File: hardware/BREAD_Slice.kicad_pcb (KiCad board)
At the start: 2 copper layers, 70 x 100 mm, 38 parts, among them J1 Conn_01x10_Socket, J2 Screw_Terminal_01x04, J3 Screw_Terminal_01x04, J4 Screw_Terminal_01x02, J5 Screw_Terminal_01x02, J6 Screw_Terminal_01x02, J7 Screw_Terminal_01x02, U1 AP63205, U2 LMD18200T_NOPB, U3 LMD18200T_NOPB

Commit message: and a few months later picked up like nothing happened...anyway done
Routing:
- net GNDPWR: track 42.2 -> 54.8 mm
- net GND: track 16.8 -> 27.3 mm, vias 20 -> 25
- net /THRM2: track 74.8 -> 81.5 mm, vias 0 -> 2
- net /DIR1: track 58.3 -> 62.7 mm
- net /CSENS2: track 73.5 -> 75.8 mm
- net /BR2: track 88.9 -> 90.9 mm, vias 0 -> 1
- net +12V: track 48.2 -> 50.1 mm, vias 0 -> 191
- net /THRM1: track 47.8 -> 49.6 mm
- net /DIR2: track 82.9 -> 84.7 mm, vias 0 -> 1
- net /PWM2: track 80.6 -> 81.6 mm
- net /BR1: track 62.5 -> 63.3 mm, vias 0 -> 1
- net /CSENS1: track 34.0 -> 34.6 mm
- net /PWM1: track 56.4 -> 56.6 mm, vias 0 -> 1
- added copper zone on B.Cu, net +12V
- added copper zone on F.Cu, net +12V

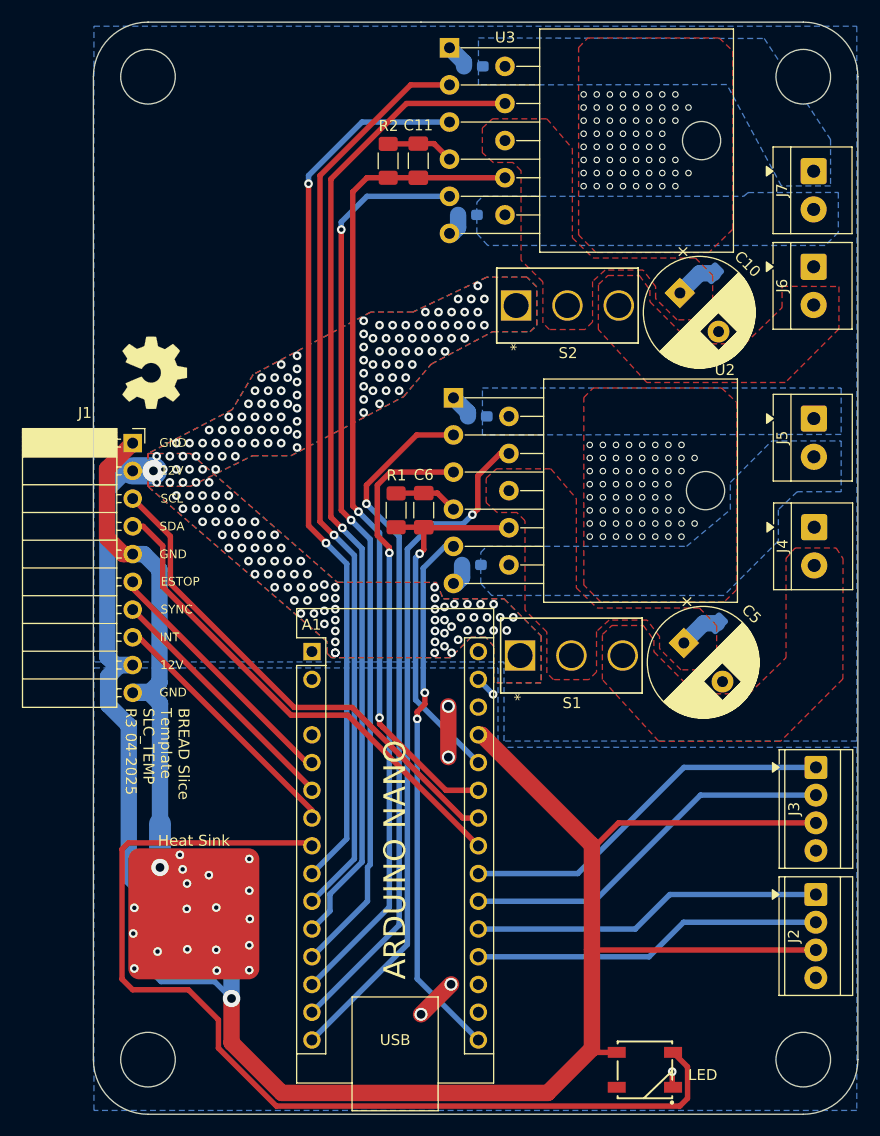
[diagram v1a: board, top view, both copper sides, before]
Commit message: review and revise for current template and kmlib
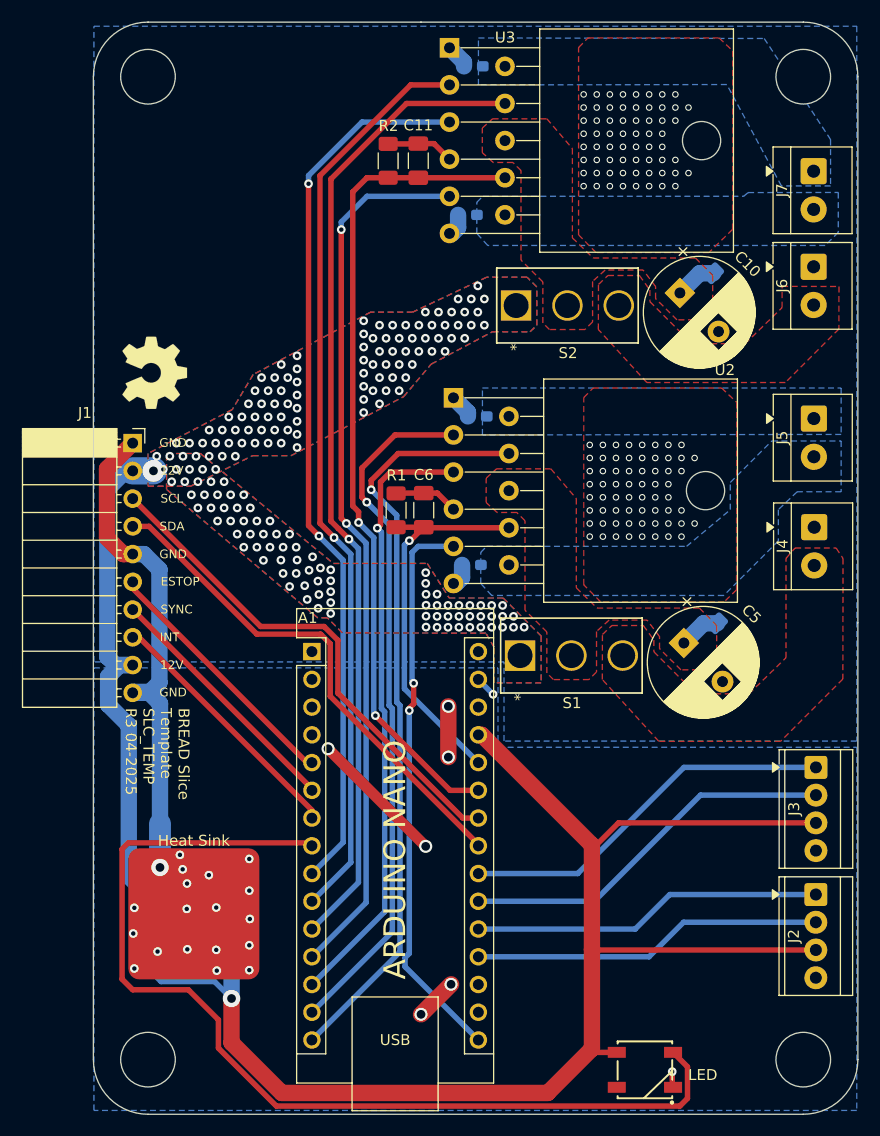
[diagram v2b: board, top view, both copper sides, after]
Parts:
- A1: footprint Module:Arduino_Nano -> KMLib_Boards_Modules:Arduino_Nano_Headers
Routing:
- net GND: track 27.3 -> 39.9 mm, vias 25 -> 27
- net /BR1: track 63.3 -> 69.3 mm
- net /THRM1: track 49.6 -> 51.8 mm
- net /DIR1: track 62.7 -> 63.7 mm
- net /CSENS1: track 34.6 -> 35.5 mm
- net /I2C_DAT: track 46.0 -> 46.7 mm
- net +12V: vias 191 -> 184
